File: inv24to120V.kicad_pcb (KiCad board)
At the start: 2 copper layers, 237.5 x 150 mm, 189 parts, among them IC1 FSAM50SM60A, J1 0705530003, J10 Screw_Terminal_01x01, J12 Screw_Terminal_01x01, J2 Conn_01x02, J3 Conn_01x02, J7 Screw_Terminal_01x03, Q1 IRFZ44NPBF, Q2 IRFZ44NPBF, Q3 ZXTN2010ZTA, Q4 ZXTN2010ZTA, Q5 ZXTP2012ZTA, Q6 ZXTP2012ZTA, SW1 SW_DIP_x02, U1 ESP32-DEVKITC-32D, U10 FOD817A, U11 ACT45B-220-2P-TL003, U12 LM2576R-5.0, U13 FOD817A, U14 KIA7805AF, U15 FOD817A, U2 LM2576R-5.0, U3 ACS712ELCTR30AT, U4 ACS712ELCTR30AT, U6 ISO7340CDW, U7 ISO7340CDW, U8 AMC1300BDWVR, U9 TJA1040T

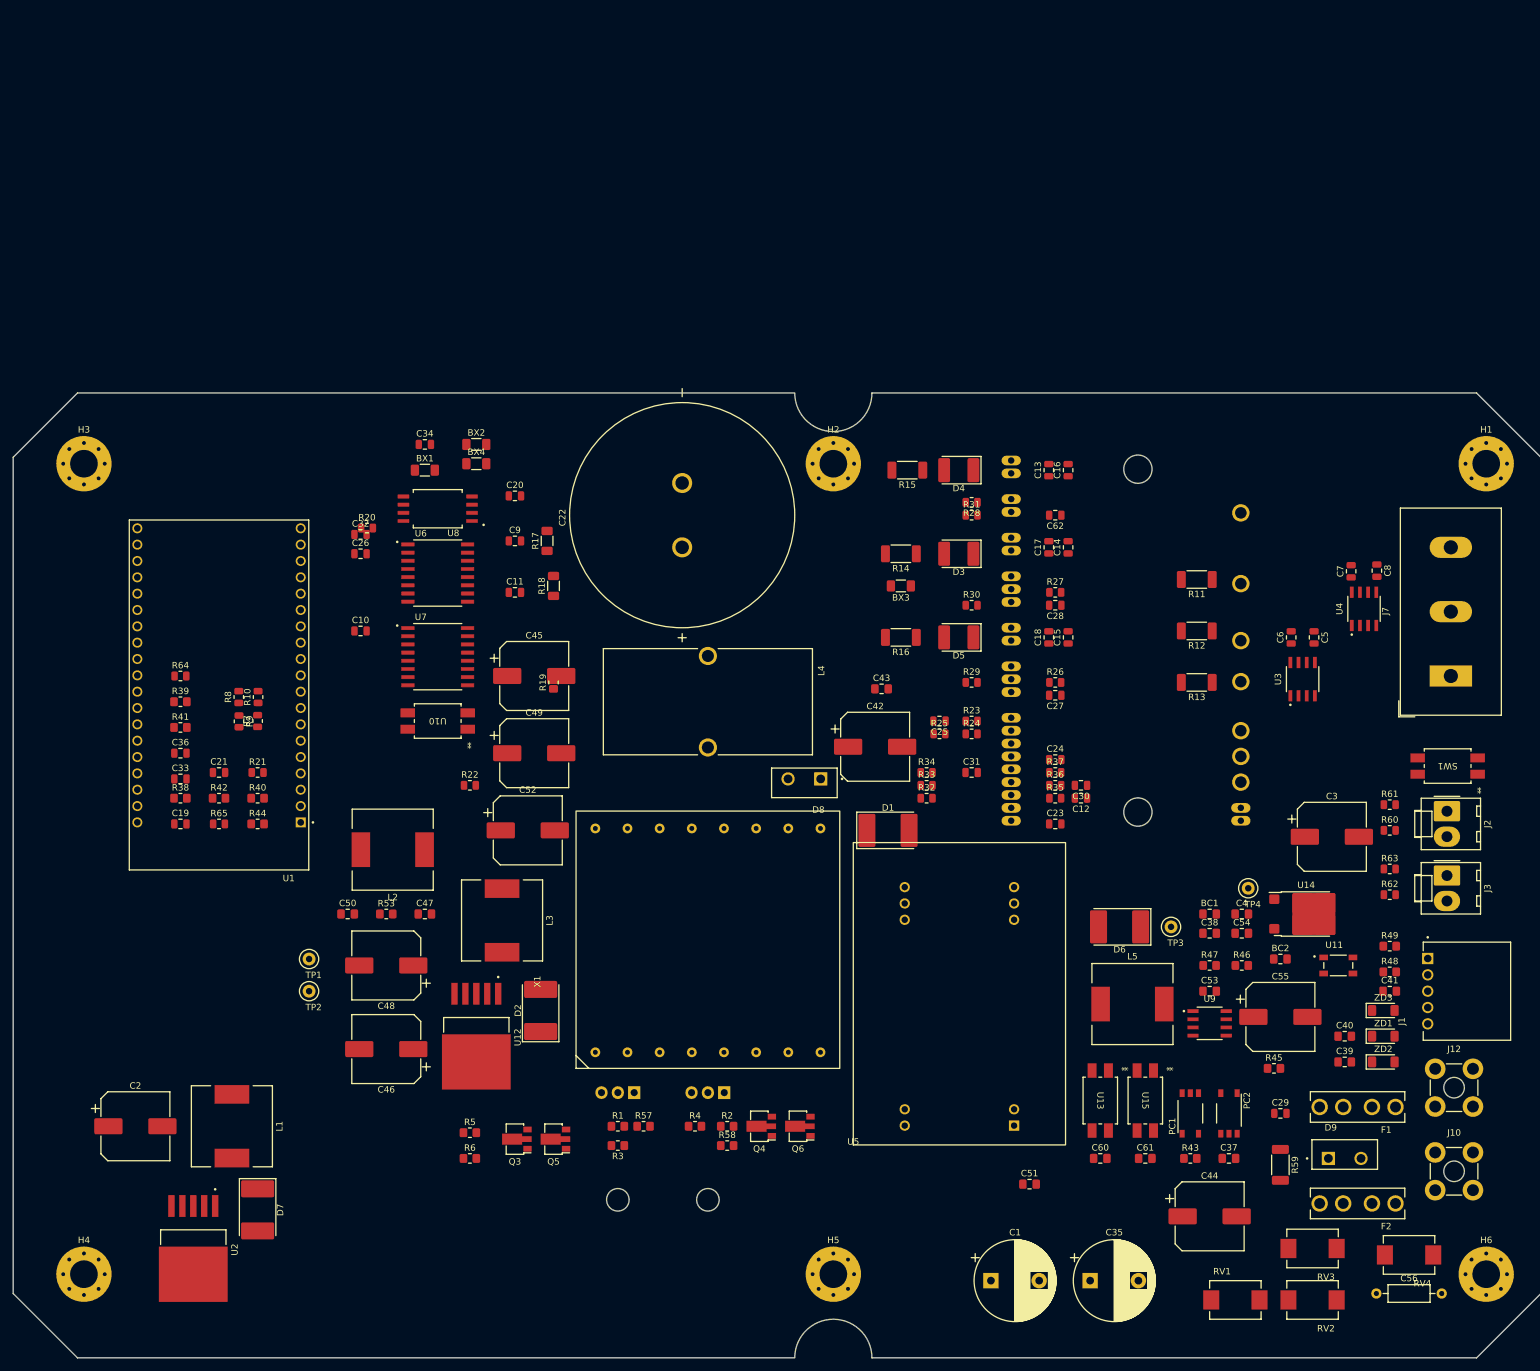
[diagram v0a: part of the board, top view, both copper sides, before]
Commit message: change IPM to STGIF7CH60TS
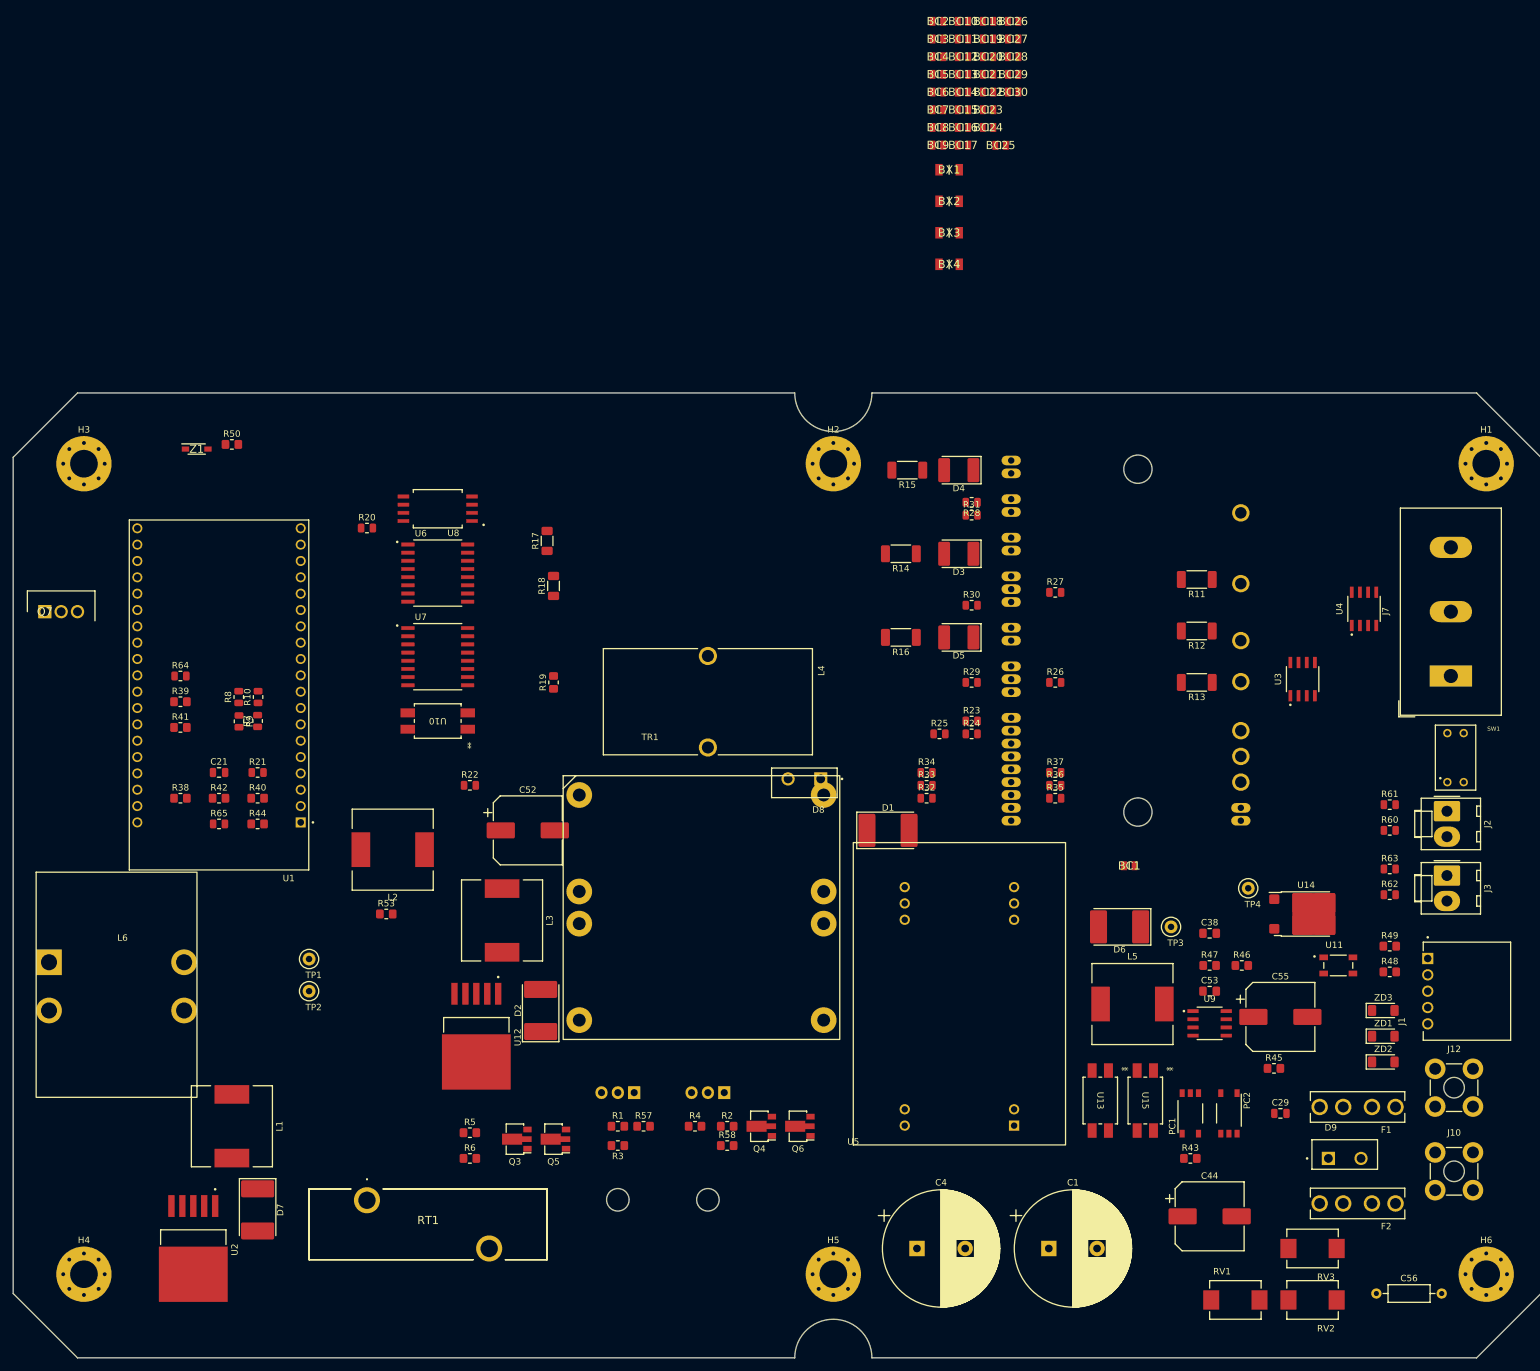
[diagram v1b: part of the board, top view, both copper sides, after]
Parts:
- removed C10, C11, C16, C17, C18, C19, C20, C23, C26, C32, C33, C34, C36, C6, C7, C9: 104, Capacitor_SMD:C_0805_2012Metric
- removed C12, C25, C27, C28, C30, C31, C5, C62, C8: 102, Capacitor_SMD:C_0805_2012Metric
- removed C13, C14, C15: 22uF/25V, Capacitor_SMD:C_0805_2012Metric
- removed C2, C3, C42, C45, C46, C48, C49: 470uF/25V, Capacitor_SMD:CP_Elec_10x12.5
- removed C22: 470uF/400V, inv24VLib:CAPPRD1000W160D3600H5200
- removed C24: 333, Capacitor_SMD:C_0805_2012Metric
- removed C35: 2200uF/50V, Capacitor_THT:CP_Radial_D12.5mm_P7.50mm
- removed C37: 103, Capacitor_SMD:C_0805_2012Metric_Pad1.18x1.45mm_HandSolder
- removed C39, C40, C41, C43, C47, C50, C51, C54, C60, C61: 104, Capacitor_SMD:C_0805_2012Metric_Pad1.18x1.45mm_HandSolder
- removed R59: 22, Resistor_SMD:R_2010_5025Metric_Pad1.40x2.65mm_HandSolder
- removed RV4: ERZ-VF2M560, inv24VLib:VAR_ERZ-VF2M560
- removed X1: ~, inv24VLib:ee42208x8p
- added BC10: 104/50V, mod:CAPC2012X95N, F.Cu at (177.7, -42.8)
- added BC11: 104/50V, mod:CAPC2012X95N, F.Cu at (177.7, -40.0)
- added BC12: 104/50V, mod:CAPC2012X95N, F.Cu at (177.7, -37.3)
- added BC13: 104/50V, mod:CAPC2012X95N, F.Cu at (177.7, -34.5)
- added BC14: 104/50V, mod:CAPC2012X95N, F.Cu at (177.7, -31.8)
- added BC15: 104/50V, mod:CAPC2012X95N, F.Cu at (177.7, -29.0)
- added BC16: 104/50V, mod:CAPC2012X95N, F.Cu at (177.7, -26.3)
- added BC17: 104/50V, mod:CAPC2012X95N, F.Cu at (177.7, -23.5)
- added BC18: 104/50V, mod:CAPC2012X95N, F.Cu at (181.6, -42.8)
- added BC19: 104/50V, mod:CAPC2012X95N, F.Cu at (181.6, -40.0)
- added BC20: 104/50V, mod:CAPC2012X95N, F.Cu at (181.6, -37.3)
- added BC21: 104/50V, mod:CAPC2012X95N, F.Cu at (181.6, -34.5)
- added BC22: 104/50V, mod:CAPC2012X95N, F.Cu at (181.6, -31.8)
- added BC23: 104/50V, mod:CAPC2012X95N, F.Cu at (181.6, -29.0)
- added BC24: 104/50V, mod:CAPC2012X95N, F.Cu at (181.6, -26.3)
- added BC25: 104/50V, mod:CAPC2012X95N, F.Cu at (183.5, -23.5)
- added BC26: 104/50V, mod:CAPC2012X95N, F.Cu at (185.4, -42.8)
- added BC27: 104/50V, mod:CAPC2012X95N, F.Cu at (185.4, -40.0)
- added BC28: 104/50V, mod:CAPC2012X95N, F.Cu at (185.4, -37.3)
- added BC29: 104/50V, mod:CAPC2012X95N, F.Cu at (185.4, -34.5)
- added BC3: 104/50V, mod:CAPC2012X95N, F.Cu at (173.8, -40.0)
- added BC30: 104/50V, mod:CAPC2012X95N, F.Cu at (185.4, -31.8)
- added BC4: 104/50V, mod:CAPC2012X95N, F.Cu at (173.8, -37.3)
- added BC5: 104/50V, mod:CAPC2012X95N, F.Cu at (173.8, -34.5)
- added BC6: 104/50V, mod:CAPC2012X95N, F.Cu at (173.8, -31.8)
- added BC7: 104/50V, mod:CAPC2012X95N, F.Cu at (173.8, -29.0)
- added BC8: 104/50V, mod:CAPC2012X95N, F.Cu at (173.8, -26.3)
- added BC9: 104/50V, mod:CAPC2012X95N, F.Cu at (173.8, -23.5)
- added L6: L_Ferrite_Coupled_1423, Inductor_THT:L_CommonMode_Toroid_Vertical_L39.4mm_W20.3mm_Px15.24mm_Py22.86mm_Bourns_8100, F.Cu at (35.6, 103.5)
- added Q7: SUP53P06-20-E3, mod:TO254P465X1028X1931-3P, F.Cu at (34.9, 49.0)
- added R50: 1K, Resistor_SMD:R_0805_2012Metric_Pad1.20x1.40mm_HandSolder, F.Cu at (64.0, 23.0)
- added RT1: MS35_1R040, mod:MS351R040, F.Cu at (85.0, 140.5)
- added TR1: pq5050v, mod:pq5050h, F.Cu at (118.0, 77.5)
- added Z1: SZMMSZ4699T1G, mod:SOD3716X135N, F.Cu at (58.5, 23.7)
- BC1, BC2: value 104 -> 104/50V; footprint Capacitor_SMD:C_0805_2012Metric_Pad1.18x1.45mm_HandSolder -> mod:CAPC2012X95N
- BX1, BX2, BX3, BX4: value BLM31KN801SH1L -> 2.5A/0.8K; footprint Resistor_SMD:R_1206_3216Metric_Pad1.30x1.75mm_HandSolder -> mod:BLM31KN102BH1L
- C1: footprint Capacitor_THT:CP_Radial_D12.5mm_P7.50mm -> Capacitor_THT:CP_Radial_D18.0mm_P7.50mm
- C21: value 104 -> 102
- C4: value 104 -> 2200uF/50V; footprint Capacitor_SMD:C_0805_2012Metric_Pad1.18x1.45mm_HandSolder -> Capacitor_THT:CP_Radial_D18.0mm_P7.50mm
- SW1: footprint inv24VLib:PDIP4GW_709AH_ONS-M -> mod:418117270902
- moved BC2 155.2 mm to (173.8, -42.8)
- moved BX1 93.9 mm to (175.5, -19.7)
- moved BX2 82.7 mm to (175.5, -14.8)
- moved BX4 79.8 mm to (175.5, -5.00)
- moved C4 72.5 mm to (170.5, 148.0)
- moved BX3 55.4 mm to (175.5, -9.90), turned to 0 degrees
- moved BC1 14.6 mm to (203.5, 88.5)
- moved C1 10.3 mm to (191.0, 148.0)
- moved SW1 1.80 mm to (254.2, 71.7), turned to 0 degrees
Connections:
- BC1 pad 1: GND1 -> +5P
- BC1 pad 2: +5P -> GND1
- BC2 pad 1: GND1 -> +5P
- BC2 pad 2: +5P -> GND1
- C4 pad 1: +8VP_IN -> +24V
- C4 pad 2: GND1 -> GND
- D8 pad 2: 150V_OUT -> 300V_OUT1
- D9 pad 1: Net-(D9-K) -> +24V
- D9 pad 2: GND -> Net-(D9-A)
- F1 pad 2_1: +24V -> Net-(F1-Pad2_1)
- F1 pad 2_2: +24V -> Net-(F1-Pad2_1)
- F2 pad 1_1: Net-(J10-Pin_1) -> unconnected-(F2-Pad1_1)
- F2 pad 2_1: GND -> Net-(BC28-Pad2)
- F2 pad 2_2: GND -> Net-(BC28-Pad2)
- RV1 pad 1: GND -> Net-(F1-Pad2_1)
- RV1 pad 2: +24V -> Net-(BC28-Pad2)
- RV2 pad 1: Net-(RV2-Pad1) -> Net-(BC28-Pad2)
- RV2 pad 2: +24V -> Earth
- RV3 pad 1: Net-(RV2-Pad1) -> Net-(F1-Pad2_1)
- RV3 pad 2: +24V -> Earth
- SW1 pad 1: GND -> DIN_B
- SW1 pad 2: GND -> DIN_A
- U2 pad 1: +24V -> GND
- U2 pad 5: GND -> +24V
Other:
- outline, holes or cut-outs redrawn

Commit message: sch design 1st done
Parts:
- removed C38: 103, Capacitor_SMD:C_0805_2012Metric_Pad1.18x1.45mm_HandSolder
- removed C52, C55: 220uF/50V, Capacitor_SMD:CP_Elec_10x12.5
- removed C53: 334, Capacitor_SMD:C_0805_2012Metric_Pad1.18x1.45mm_HandSolder
- removed C56: 102/1kV, Resistor_THT:R_Axial_DIN0207_L6.3mm_D2.5mm_P10.16mm_Horizontal
- removed D1, D2, D6, D7: SS16, Diode_SMD:D_3220_8050Metric_Pad2.65x5.15mm_HandSolder
- removed D3, D4, D5: ES1F-ES1J, Diode_SMD:D_2114_3652Metric_Pad1.85x3.75mm_HandSolder
- removed D8: BYV29X-500, inv24VLib:TO507P1020X460X2000-2
- removed F1, F2: 3544-2, inv24VLib:FUSE_3544-2

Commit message: start place component
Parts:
- removed BC20, BC21, BC22, BC24, BC25, BC26, BC27, BC28, BC29, BC30: 104/50V, mod:CAPC2012X95N
- removed C29: 104, Capacitor_SMD:C_0805_2012Metric
- removed C44: 470uF/25V, Capacitor_SMD:CP_Elec_10x12.5
- removed D9: BYV29X-500, inv24VLib:TO507P1020X460X2000-2
- removed J10: Screw_Terminal_01x01, TerminalBlock_Wuerth:Wuerth_REDCUBE-THR_WP-THRBU_74650073_THR
- removed J7: Screw_Terminal_01x03, TerminalBlock_Dinkle:TerminalBlock_Dinkle_DT-55-B01X-03_P10.00mm
- removed L6: L_Ferrite_Coupled_1423, Inductor_THT:L_CommonMode_Toroid_Vertical_L39.4mm_W20.3mm_Px15.24mm_Py22.86mm_Bourns_8100
- removed PC1, PC2: TLP115A, Package_SO:MFSOP6-5_4.4x3.6mm_P1.27mm
- removed R36, R37: 4.7K, Resistor_SMD:R_0805_2012Metric
- removed R39: 2K, Resistor_SMD:R_0805_2012Metric_Pad1.20x1.40mm_HandSolder
- removed R50: 1K, Resistor_SMD:R_0805_2012Metric_Pad1.20x1.40mm_HandSolder
- removed R53: 1k, Resistor_SMD:R_0805_2012Metric_Pad1.20x1.40mm_HandSolder
- removed R57, R58: 10, Resistor_SMD:R_0805_2012Metric_Pad1.20x1.40mm_HandSolder
- removed R60, R62: 470, Resistor_SMD:R_0805_2012Metric
- removed R61, R63, R64, R65: 10K, Resistor_SMD:R_0805_2012Metric
- removed TP1, TP2, TP3, TP4: TestPoint, TestPoint:TestPoint_Loop_D2.50mm_Drill1.0mm
- removed U10, U13: FOD817A, inv24VLib:PDIP4GW_709AH_ONS-M
- removed U11: ACT45B-220-2P-TL003, genCtrlPCB_Lib:FIL_ACT45B-220-2P-TL003
- removed U12: LM2576R-5.0, genCtrlPCB_Lib:VREG_TPS79625KTTR
- removed U14: KIA7805AF, Package_TO_SOT_SMD:ATPAK-2
- removed U6, U7: ISO7340CDW, inv24VLib:SOIC127P1030X265-16N
- removed U8: AMC1300BDWVR, inv24VLib:SOIC127P1150X280-8N
- removed U9: TJA1040T, genCtrlPCB_Lib:SOIC127P600X175-8N
- removed ZD1, ZD2, ZD3: ZMM55C27, Diode_SMD:D_MiniMELF
- added BX5: 2.5A/0.8K, mod:BLM31KN102BH1L, F.Cu at (141.0, 29.0)
- added C10: 102, Capacitor_SMD:C_0805_2012Metric, F.Cu at (68.0, 62.5)
- added C11: 2.2uF/50V, Capacitor_SMD:C_1206_3216Metric_Pad1.33x1.80mm_HandSolder, F.Cu at (151.0, -11.0)
- added C12: 102, Capacitor_SMD:C_0805_2012Metric, F.Cu at (170.4, 108.2)
- added C13: 104, Capacitor_SMD:C_0805_2012Metric, F.Cu at (56.5, 58.0)
- added C14: 104, Capacitor_SMD:C_0805_2012Metric, F.Cu at (174.9, 102.2)
- added C15: 680uF/25V, Capacitor_SMD:CP_Elec_16x17.5, F.Cu at (64.0, 186.0)
- added C16: 2.2uF/50V, Capacitor_SMD:C_1206_3216Metric_Pad1.33x1.80mm_HandSolder, F.Cu at (151.0, -3.00)
- added C17: 680uF/25V, Capacitor_SMD:CP_Elec_16x17.5, F.Cu at (91.0, 185.5)
- added C18: 2.2uF/50V, Capacitor_SMD:C_1206_3216Metric_Pad1.33x1.80mm_HandSolder, F.Cu at (203.0, 92.0)
- added C19: 2.2uF/50V, Capacitor_SMD:C_1206_3216Metric_Pad1.33x1.80mm_HandSolder, F.Cu at (240.5, 91.5)
- added C2: 680uF/25V, Capacitor_SMD:CP_Elec_16x17.5, F.Cu at (116.5, 185.5)
- added C20: 473, Capacitor_SMD:C_0805_2012Metric, F.Cu at (228.0, 100.0)
- added C22: 470uF/400V, Capacitor_THT:CP_Radial_D35.0mm_P10.00mm_SnapIn, F.Cu at (112.6, 27.0)
- added C23: 4.7p, Capacitor_SMD:C_0805_2012Metric, F.Cu at (243.0, 104.0)
- added C27: 102, Capacitor_SMD:C_0805_2012Metric, F.Cu at (174.9, 111.2)
- added C28: 102, Capacitor_SMD:C_0805_2012Metric, F.Cu at (179.3, 102.2)
- added C3: 2.2uF/50V, Capacitor_SMD:C_1206_3216Metric_Pad1.33x1.80mm_HandSolder, F.Cu at (198.0, 84.0)
- added C30: 102, Capacitor_SMD:C_0805_2012Metric, F.Cu at (179.3, 105.2)
- added C31: 102, Capacitor_SMD:C_0805_2012Metric, F.Cu at (179.3, 108.2)
- added C5: 102, Capacitor_SMD:C_0805_2012Metric, F.Cu at (68.0, 49.0)
- added C56: 102/1kV, Capacitor_SMD:C_1812_4532Metric_Pad1.57x3.40mm_HandSolder, F.Cu at (246.0, 161.0)
- added C6: 680uF/25V, Capacitor_SMD:CP_Elec_16x17.5, F.Cu at (40.5, 187.0)
- added C62: 102, Capacitor_SMD:C_0805_2012Metric, F.Cu at (179.3, 111.2)
- added C7: 2.2uF/50V, Capacitor_SMD:C_1206_3216Metric_Pad1.33x1.80mm_HandSolder, F.Cu at (197.0, 27.0)
- added C8: 2.2uF/50V, Capacitor_SMD:C_1206_3216Metric_Pad1.33x1.80mm_HandSolder, F.Cu at (205.5, 33.5)
- added C9: 2.2uF/50V, Capacitor_SMD:C_1206_3216Metric_Pad1.33x1.80mm_HandSolder, F.Cu at (198.0, 39.5)
- added D1: BYV29X-600, mod:TO507P1020X460X2000-2, F.Cu at (228.0, 135.5)
- added D10: BAT48J, Diode_SMD:D_SOD-323_HandSoldering, F.Cu at (209.5, 63.0)
- added D11: BAT48J, Diode_SMD:D_SOD-323_HandSoldering, F.Cu at (209.5, 59.5)
- added D12: BAT48J, Diode_SMD:D_SOD-323_HandSoldering, F.Cu at (209.5, 56.0)
- added D13: 15V/1W, Diode_SMD:D_SMA_Handsoldering, F.Cu at (199.0, 33.0)
- added D14: BAT48J, Diode_SMD:D_SOD-323_HandSoldering, F.Cu at (69.0, 66.5)
- added D2: 15V/1W, Diode_SMD:D_SMA_Handsoldering, F.Cu at (199.5, 37.0)
- added D3: SS26, mod:DIOM5127X229N, F.Cu at (185.5, 102.8)
- added D4: SS26, mod:DIOM5127X229N, F.Cu at (185.5, 107.2)
- added D5: 15V/1W, Diode_SMD:D_SMA_Handsoldering, F.Cu at (199.5, 29.0)
- added D7: SS26, mod:DIOM5127X229N, F.Cu at (185.5, 111.5)
- added D8: BYV29X-600, mod:TO507P1020X460X2000-2, F.Cu at (136.5, 44.5)
- added F1: 3544-2, mod:FUSE_3544-2, F.Cu at (242.5, 120.0)
- added F2: 3544-2, mod:FUSE_3544-2, F.Cu at (243.5, 139.0)
- added F3: 7A/350V, Fuse:Fuse_2920_7451Metric_Pad2.10x5.45mm_HandSolder, F.Cu at (234.5, 27.5)
- added F4: 7A/350V, Fuse:Fuse_2920_7451Metric_Pad2.10x5.45mm_HandSolder, F.Cu at (234.5, 38.5)
- added F5: 7A/350V, Fuse:Fuse_2920_7451Metric_Pad2.10x5.45mm_HandSolder, F.Cu at (234.5, 47.0)
- added FL1: ACT45B-510-2P-TL003, mod:ACT45B1012PTL003, F.Cu at (249.0, 109.0)
- added IC2: ISO7221AQDRQ1, mod:SOIC127P600X175-8N, F.Cu at (230.5, 109.0)
- added J4: Screw_Terminal_01x03, TerminalBlock_Dinkle:TerminalBlock_Dinkle_DT-55-B01X-03_P10.00mm, F.Cu at (256.5, 40.5)
- added J5: BR-120, TerminalBlock_Wuerth:Wuerth_REDCUBE-THR_WP-THRBU_74650073_THR, F.Cu at (258.5, 135.5)
- added LED1: LTST-C170GKT, mod:LEDC2012X120N, F.Cu at (258.0, 111.0)
- added LED2: LTST-C170GKT, mod:LEDC2012X120N, F.Cu at (258.0, 109.0)
- added PS1: NTE0505MC, mod:NTE0505MC, F.Cu at (215.0, 89.0)
- added Q8: STGIF7CH60TS-L, mod:STGIB20M60TSL, F.Cu at (191.9, 29.8)
- added R51: 4.7K, Resistor_SMD:R_1206_3216Metric_Pad1.30x1.75mm_HandSolder, F.Cu at (63.0, 46.0)
- added Z2: SMAJ40AHE3_A/H, mod:DIOM5027X244N, F.Cu at (247.0, 97.0)
- added Z3: SMAJ40AHE3_A/H, mod:DIOM5027X244N, F.Cu at (247.0, 101.0)
- C21: value 102 -> 4.7p
- IC1: value FSAM50SM60A -> MCP2551-E_SN; footprint inv24VLib:DIP-32 -> mod:SOIC127P600X175-8N; moved to F.Cu
- J1: value 0705530003 -> 70543-0003; footprint genCtrlPCB_Lib:MOLEX_0705530039 -> mod:SHDR4W97P0X254_1X4_1271X660X1143P
- J12: value Screw_Terminal_01x01 -> BR-120
- J2, J3: value Conn_01x02 -> 70543-0001; footprint Connector_Molex:Molex_KK-396_A-41791-0002_1x02_P3.96mm_Vertical -> mod:SHDR2W64P0X254_1X2_737X660X1181P
- L1, L2, L3, L5: footprint Inductor_SMD:L_12x12mm_H8mm -> mod:INDPM120120X600N
- L4: footprint inv24VLib:IND_HCTI-10-20.0 -> mod:IND_HCTI-10-20.0
- R10: value 2K -> 1.0K; footprint Resistor_SMD:R_0805_2012Metric -> Resistor_SMD:R_1206_3216Metric_Pad1.30x1.75mm_HandSolder
- R11: value 5.6 -> 12K; footprint Resistor_SMD:R_2010_5025Metric_Pad1.40x2.65mm_HandSolder -> Resistor_SMD:R_1206_3216Metric_Pad1.30x1.75mm_HandSolder
- R12: value 5.6 -> 10K; footprint Resistor_SMD:R_2010_5025Metric_Pad1.40x2.65mm_HandSolder -> Resistor_SMD:R_0805_2012Metric_Pad1.20x1.40mm_HandSolder
- R13: value 5.6 -> 120; footprint Resistor_SMD:R_2010_5025Metric_Pad1.40x2.65mm_HandSolder -> Resistor_SMD:R_0805_2012Metric_Pad1.20x1.40mm_HandSolder
- R14, R15, R16: value 22 -> 120; footprint Resistor_SMD:R_2010_5025Metric_Pad1.40x2.65mm_HandSolder -> Resistor_SMD:R_0805_2012Metric_Pad1.20x1.40mm_HandSolder
- R17, R18: value 1M/2W -> 500K/3216
- R19: value 1K -> 1.0K; footprint Resistor_SMD:R_0805_2012Metric_Pad1.20x1.40mm_HandSolder -> Resistor_SMD:R_1206_3216Metric_Pad1.30x1.75mm_HandSolder
- R20, R21: value 2K -> 0; footprint Resistor_SMD:R_0805_2012Metric -> Resistor_SMD:R_0805_2012Metric_Pad1.20x1.40mm_HandSolder
- R22, R29, R30, R31, R32, R33, R34: footprint Resistor_SMD:R_0805_2012Metric -> Resistor_SMD:R_0805_2012Metric_Pad1.20x1.40mm_HandSolder
- R23: value 390 -> 470; footprint Resistor_SMD:R_0805_2012Metric -> Resistor_SMD:R_0805_2012Metric_Pad1.20x1.40mm_HandSolder
- R24: value 3.9K -> 10; footprint Resistor_SMD:R_0805_2012Metric -> Resistor_SMD:R_0805_2012Metric_Pad1.20x1.40mm_HandSolder
- R25: value 45 -> 10; footprint Resistor_SMD:R_0805_2012Metric -> Resistor_SMD:R_0805_2012Metric_Pad1.20x1.40mm_HandSolder
- R26, R27, R28: value 4.7K -> 1.0K; footprint Resistor_SMD:R_0805_2012Metric -> Resistor_SMD:R_1206_3216Metric_Pad1.30x1.75mm_HandSolder
- R35: value 4.7K -> 2.0K; footprint Resistor_SMD:R_0805_2012Metric -> Resistor_SMD:R_1206_3216Metric_Pad1.30x1.75mm_HandSolder
- R41: value 100 -> 500K/3216; footprint Resistor_SMD:R_0805_2012Metric_Pad1.20x1.40mm_HandSolder -> Resistor_SMD:R_1206_3216Metric_Pad1.30x1.75mm_HandSolder
- R42: value 1K -> 10K
- R43: value 120 -> 10K
- R44: value 4.7K -> 10K
- R45: value 220 -> 100
- R46: value 470 -> 500K/3216; footprint Resistor_SMD:R_0805_2012Metric_Pad1.20x1.40mm_HandSolder -> Resistor_SMD:R_1206_3216Metric_Pad1.30x1.75mm_HandSolder
- R47: value 0 -> 1.0K; footprint Resistor_SMD:R_0805_2012Metric_Pad1.20x1.40mm_HandSolder -> Resistor_SMD:R_1206_3216Metric_Pad1.30x1.75mm_HandSolder
- R48, R49: value 60 -> 470
- R7, R8, R9: value 2K -> 0.08/2W; footprint Resistor_SMD:R_0805_2012Metric -> Resistor_SMD:R_2816_7142Metric_Pad3.20x4.45mm_HandSolder
- RV1, RV2, RV3: footprint inv24VLib:VAR_ERZ-VF2M560 -> mod:VAR_ERZ-VF2M560
- U15: value FOD817A -> FOD817A3SD; footprint inv24VLib:PDIP4GW_709AH_ONS-M -> mod:PDIP4GW_709AH_ONS-M
- U2: value LM2576R-5.0 -> LM2576D2T-15G; footprint genCtrlPCB_Lib:VREG_TPS79625KTTR -> mod:KTT0005B
- U3: value ACS712ELCTR30AT -> LM2576-3.3WU; footprint inv24VLib:SOIC127P600X175-8N -> mod:KTT0005B
- U4: value ACS712ELCTR30AT -> LM2576D2TR4-5G; footprint inv24VLib:SOIC127P600X175-8N -> mod:KTT0005B
- U5: value ~ -> FOD817A3SD; footprint Library:ewDCDC24_1505d -> mod:PDIP4GW_709AH_ONS-M
- moved U3 198.0 mm to (39.0, 110.0)
- moved U4 195.4 mm to (54.5, 110.0)
- moved R42 181.0 mm to (243.0, 78.0)
- moved C21 178.5 mm to (238.0, 104.0)
- moved R43 178.5 mm to (55.0, 51.0)
- moved R21 168.0 mm to (234.0, 100.0)
- moved R9 168.0 mm to (233.0, 70.5), turned to 0 degrees
- moved R8 167.9 mm to (233.0, 64.5), turned to 0 degrees
- moved R20 165.8 mm to (238.0, 100.0)
- moved R7 165.2 mm to (233.0, 58.0), turned to 0 degrees
- moved R11 158.4 mm to (56.5, 61.0)
- moved R45 157.0 mm to (83.5, 54.0)
- moved BC1 153.9 mm to (55.0, 48.0)
- moved R22 153.0 mm to (251.0, 106.0)
- moved BC2 152.7 mm to (246.5, 91.5)
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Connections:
- net SCI_RXD renamed CAN_RXD
- net SCI_TXD renamed CAN_TXD
- BC1 pad 1: +5P -> DIN_A
- BC1 pad 2: GND1 -> GND
- BC10 pad 1: Net-(D3-K) -> +24V
- BC10 pad 2: Net-(IC1-VS(V)) -> GND
- BC11 pad 1: Net-(D5-K) -> +24V
- BC11 pad 2: Net-(IC1-VS(U)) -> GND
- BC13 pad 1: +5VP -> +24V
- BC13 pad 2: GND2 -> GND
- BC14 pad 1: +15V -> +24V
- BC14 pad 2: GND2 -> GND
- BC15 pad 1: +3.3V -> +5P
- BC15 pad 2: GND -> GND1
- BC16 pad 1: +5V -> +3.3V
- BC17 pad 1: VTH_IPM -> DIN_B
- BC17 pad 2: Net-(BC17-Pad2) -> GND
- BC18 pad 1: TEMPERATURE_IPM -> +5V
- BC19 pad 1: +5V -> Net-(D1-A)
- BC23 pad 1: 15V_H_IN -> +15V
- BC3 pad 1: +8VP_IN -> +5P
- BC4 pad 1: GND -> VBOOT_U
- BC4 pad 2: +5V -> PHASE_U
- BC5 pad 1: +5V -> VBOOT_V
- BC5 pad 2: GND -> PHASE_V
- BC6 pad 1: +5VP -> VBOOT_W
- BC6 pad 2: GND2 -> PHASE_W
- BC7 pad 1: +3.3V -> +15V
- BC7 pad 2: GND -> GND2
- BC8 pad 1: +5VP -> Net-(BC8-Pad1)
- BC8 pad 2: GND2 -> GNDPWR
- BC9 pad 1: Net-(D4-K) -> VDC_sensor
- BC9 pad 2: Net-(IC1-VS(W)) -> GND
- BX1 pad 1: +5V -> GND
- BX1 pad 2: VTH_IPM -> GNDPWR
- BX2 pad 1: GND -> Net-(BX2-Pad1)
- BX2 pad 2: Net-(BC17-Pad2) -> +5V
- BX3 pad 1: GND2 -> GND
- BX4 pad 1: TEMPERATURE_IPM -> Net-(BX4-Pad1)
- BX4 pad 2: Net-(IC1-RTH) -> GND
- C21 pad 1: GND -> Net-(IC1-CANH)
- C21 pad 2: VDC_sensor -> GND1
- IC1 pad 1: +15V -> Net-(IC1-TXD)
- IC1 pad 2: GND2 -> GND1
- IC1 pad 3: IN_UL -> +5P
- IC1 pad 4: IN_VL -> Net-(IC1-RXD)
- IC1 pad 5: IN_WL -> Net-(IC1-VREF)
- IC1 pad 6: GND2 -> Net-(IC1-CANL)
- IC1 pad 7: Net-(IC1-VFO) -> Net-(IC1-CANH)
- IC1 pad 8: Net-(IC1-CFOD) -> GND1
- J1 pad 3: Net-(ZD1-K) -> Net-(Z3-K)
- J1 pad 4: Net-(ZD3-K) -> Net-(Z2-K)
- J2 pad 2: Net-(J2-Pin_2) -> Net-(J2-Pad2)
- J3 pad 2: Net-(J3-Pin_2) -> Net-(J3-Pad2)
- L1 pad 2: +5V -> +15V
- L2 pad 1: Net-(D2-K) -> Net-(D4-K)
- L2 pad 2: +5VP -> +5V
- L3 pad 1: Net-(D1-K) -> Net-(D3-K)
- L3 pad 2: Net-(U12-VIN) -> +3.3V
- L5 pad 2: +BATT -> +5P
- Q7 pad 2: Net-(D9-A) -> Net-(D1-A)
- R1 pad 1: Net-(Q3-E) -> Net-(Q1-G)
- R1 pad 2: Net-(Q1-G) -> Net-(Q3-E)
- R10 pad 1: GND -> Net-(D10-A)
- R10 pad 2: I_Vphase -> Net-(Q8-NW)
- R11 pad 1: /W_phase -> T2
- R11 pad 2: Net-(IC1-VS(W)) -> GND
- R12 pad 1: V_sensor -> +3.3V
- R12 pad 2: Net-(IC1-VS(V)) -> SD
- R13 pad 1: U_sensor -> Net-(R13-Pad1)
- R13 pad 2: Net-(IC1-VS(U)) -> Net-(IC1-VREF)
- R14 pad 1: Net-(D3-A) -> Net-(R13-Pad1)
- R14 pad 2: +15V -> Net-(IC1-VREF)
- R15 pad 1: Net-(D4-A) -> Net-(R15-Pad1)
- R15 pad 2: +15V -> Net-(IC1-VREF)
- R16 pad 1: Net-(D5-A) -> Net-(R15-Pad1)
- R16 pad 2: +15V -> Net-(IC1-VREF)
- R17 pad 2: VBUS -> Net-(R17-Pad2)
- R18 pad 1: Net-(U8-INP) -> Net-(R18-Pad1)
- R18 pad 2: Net-(R17-Pad1) -> Net-(R17-Pad2)
- R19 pad 1: GNDPWR -> Net-(BC8-Pad1)
- R19 pad 2: Net-(U8-INP) -> GNDPWR
- R2 pad 1: Net-(Q4-E) -> Net-(Q2-G)
- R2 pad 2: Net-(Q2-G) -> Net-(Q4-E)
- R20 pad 1: VDC_sensor -> Net-(IC1-CANH)
- R20 pad 2: Net-(U8-OUTP) -> Net-(R13-Pad1)
- R21 pad 1: GND -> Net-(IC1-CANL)
- R21 pad 2: VDC_sensor -> Net-(R15-Pad1)
- R22 pad 1: Net-(R22-Pad1) -> +3.3V
- R22 pad 2: +5VP -> Net-(LED2-A)
- R23 pad 1: Net-(C25-Pad1) -> +3.3V
- R23 pad 2: Net-(IC1-CSC) -> Net-(LED1-A)
- R24 pad 1: Net-(C25-Pad1) -> Net-(Q2-G)
- R24 pad 2: Net-(IC1-RSC) -> Net-(Q6-E)
- R25 pad 1: GND2 -> Net-(Q1-G)
- R25 pad 2: Net-(IC1-RSC) -> Net-(Q5-E)
- R26 pad 1: IN_UH -> Net-(D11-A)
- R26 pad 2: +5VP -> Net-(Q8-NV)
- R27 pad 1: IN_VH -> Net-(D12-A)
- R27 pad 2: +5VP -> Net-(Q8-NU)
- R28 pad 1: IN_WH -> CIN
- R28 pad 2: +5VP -> Net-(D10-K)
- R29 pad 1: UH1 -> IN_UH
- R29 pad 2: IN_UH -> PWM0_H
- R3 pad 1: GND -> Net-(Q1-G)
- R3 pad 2: Net-(Q1-G) -> GND
- R30 pad 1: VH1 -> IN_VH
- R30 pad 2: IN_VH -> PWM1_H
- R31 pad 1: WH1 -> IN_WH
- R31 pad 2: IN_WH -> PWM2_H
- R32 pad 1: UL1 -> IN_VL
- R32 pad 2: IN_UL -> PWM1_L
- R33 pad 1: VL1 -> IN_WL
- R33 pad 2: IN_VL -> PWM2_L
- R34 pad 1: WL1 -> Net-(R34-Pad1)
- R34 pad 2: IN_WL -> GND
- R35 pad 1: IN_UL -> Net-(R34-Pad1)
- R35 pad 2: +5VP -> +24V
- R38 pad 1: Net-(R38-Pad1) -> VDC_IN
- R38 pad 2: VDC_IN -> Net-(R34-Pad1)
- R4 pad 1: GND -> Net-(Q2-G)
- R4 pad 2: Net-(Q2-G) -> GND
- R40 pad 1: GND -> Net-(R40-Pad1)
- R40 pad 2: TEMPERATURE_IPM -> GND1
- R41 pad 1: GND -> VBUS
- R41 pad 2: Net-(R38-Pad1) -> Net-(R17-Pad1)
- R42 pad 1: +3.3V -> Net-(R42-Pad1)
- R42 pad 2: RX_CAN -> GND1
- R43 pad 1: Net-(PC1-Pad1) -> +3.3V
- R43 pad 2: +3.3V -> DIN_A
- R44 pad 2: FAULT_IPM -> DIN_B
- R45 pad 1: Net-(PC2-Pad1) -> IN_UL
- R45 pad 2: +5P -> PWM0_L
- R46 pad 1: +5P -> Net-(BC8-Pad1)
- R46 pad 2: Net-(U9-TXD) -> Net-(R18-Pad1)
- R47 pad 1: Net-(BC20-Pad1) -> Net-(Q7-G)
- R47 pad 2: Net-(U9-SPLIT) -> GND
- R48 pad 1: Net-(BC20-Pad1) -> Net-(J2-Pad2)
- R48 pad 2: Net-(ZD1-K) -> Net-(R40-Pad1)
- R49 pad 1: Net-(BC20-Pad1) -> Net-(J3-Pad2)
- R49 pad 2: Net-(ZD3-K) -> Net-(R42-Pad1)
- R5 pad 1: PWM_A -> Net-(Q3-B)
- R5 pad 2: Net-(Q3-B) -> PWM_A
- R6 pad 1: PWM_B -> Net-(Q4-B)
- R6 pad 2: Net-(Q4-B) -> PWM_B
- R7 pad 1: I_Uphase -> Net-(Q8-NU)
- R7 pad 2: Net-(U3-VIOUT) -> GNDPWR
- R8 pad 1: I_Vphase -> Net-(Q8-NV)
- R8 pad 2: Net-(U4-VIOUT) -> GNDPWR
- R9 pad 1: GND -> Net-(Q8-NW)
- R9 pad 2: I_Uphase -> GNDPWR
- RT1 pad 2: Net-(BC28-Pad1) -> Net-(D1-A)
- RV1 pad 2: Net-(BC28-Pad2) -> GND
- RV2 pad 1: Net-(BC28-Pad2) -> Net-(F1-Pad2_1)
- RV3 pad 1: Net-(F1-Pad2_1) -> GND
- U1 pad J3-10: unconnected-(U1-IO5-PadJ3-10) -> FAULT_IPM
- U1 pad J3-2: FAULT_IPM -> CIN
- U15 pad 1: Net-(R62-Pad1) -> Net-(R42-Pad1)
- U2 pad 4: +5V -> +15V
- U3 pad 1: U_sensor -> GND
- U3 pad 2: U_sensor -> Net-(D3-K)
- U3 pad 3: U_phase -> GND
- U3 pad 4: U_phase -> +3.3V
- U3 pad 5: GND -> +24V
- U3 pad 6: Net-(U3-FILTER) -> GND
- U3 pad 7: Net-(U3-VIOUT) -> (no net)
- U3 pad 8: +5V -> (no net)
- U4 pad 1: V_sensor -> GND
- U4 pad 2: V_sensor -> Net-(D4-K)
- U4 pad 3: V_phase -> GND
- U4 pad 4: V_phase -> +5V
- U4 pad 5: GND -> +24V
- U4 pad 6: Net-(U4-FILTER) -> GND
- U4 pad 7: Net-(U4-VIOUT) -> (no net)
- U4 pad 8: +5V -> (no net)
- U5 pad 1: +24V -> Net-(R40-Pad1)
- U5 pad 2: GND -> GND1
- U5 pad 3: unconnected-(U5-NC1-Pad3) -> GND
- U5 pad 4: unconnected-(U5-NC2-Pad4) -> DIN_A
